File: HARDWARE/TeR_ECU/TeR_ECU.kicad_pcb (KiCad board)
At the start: 4 copper layers, 108.5 x 67.8 mm, 166 parts, among them IC1 MX34040NF2, J1 RJ45_Shielded, J2 RJ45_Shielded, J3 DEBUG, J4 USB_B_Mini, J5 GPS_ANT, K2 G5Q-1, Q1 ZXMN3F30FH, Q2 ZXMN3F30FH, Q3 ZXMN3F30FH, Q4 ZXMN3F30FH, Q5 ZXMN3F30FH, SW1 RST, SW2 BOOT0, U1 TCAN332, U10 NEO-M9N, U11 AT24CS02-STUM, U2 TCAN332, U3 TSR_1-2450, U4 LM1117MP-3.3, U5 LM324, U6 STM32F405VGTx, U7 USBLC6-2SC6, U8 ASM330LHH, U9 LIS3MDL, Y2 ECS-250-20-33-CKM-TR

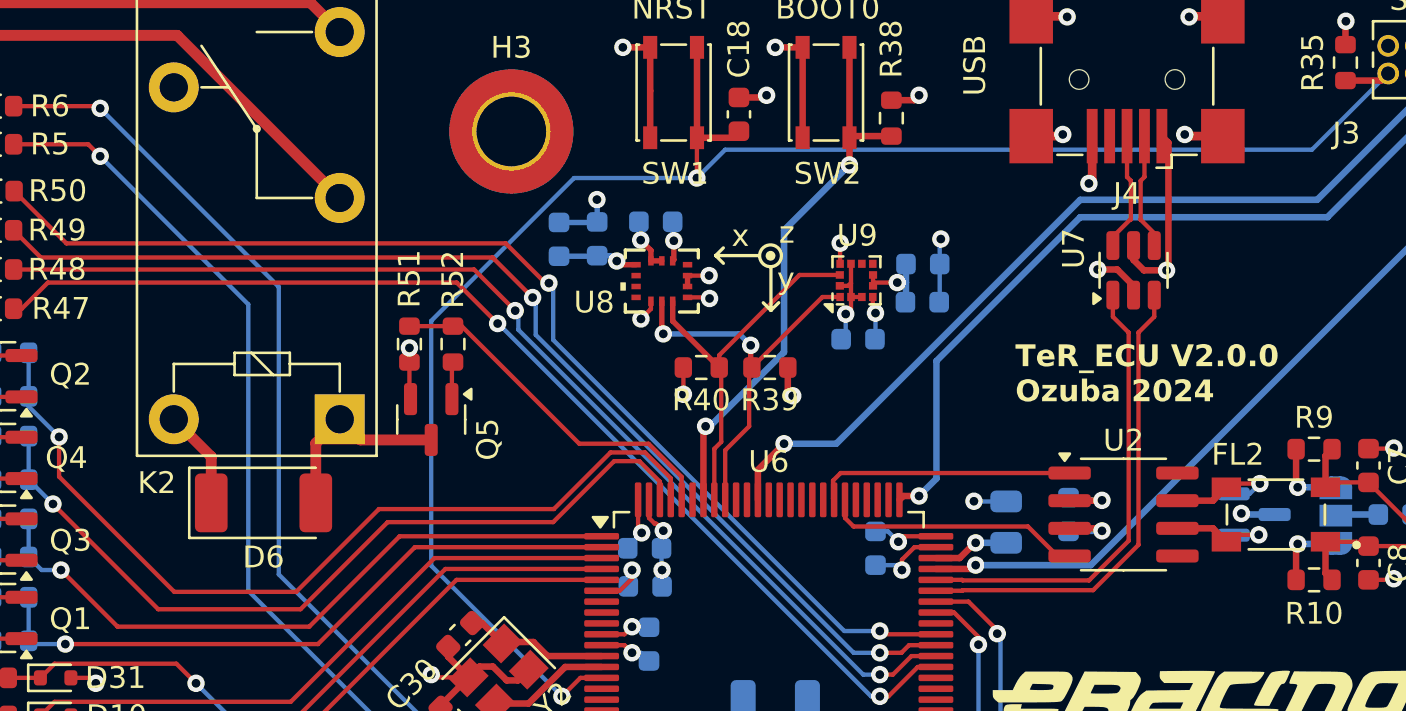
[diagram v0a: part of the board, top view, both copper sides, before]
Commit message: Added Diode to clamp usb pwr
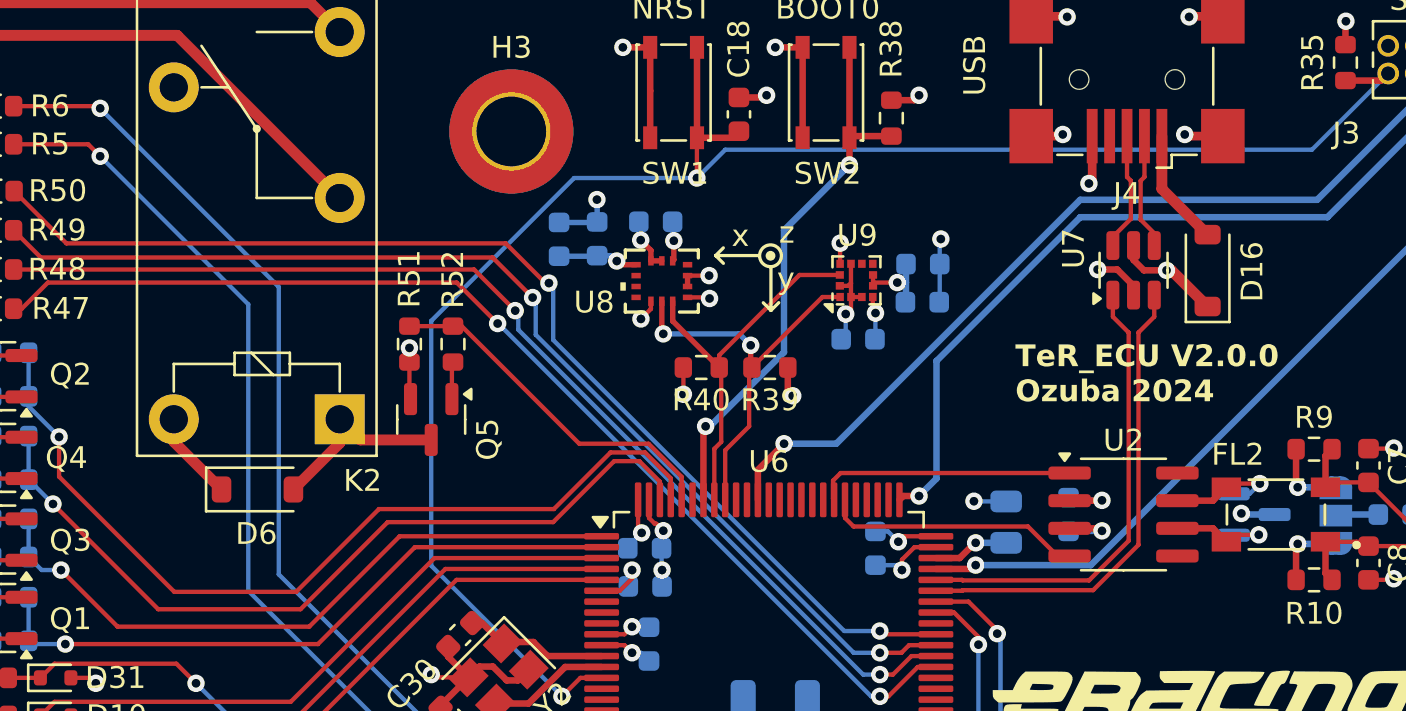
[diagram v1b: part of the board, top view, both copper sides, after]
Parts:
- added D16: SS14, Diode_SMD:D_SOD-123, F.Cu at (170.7, 72.0)
- D6: value SM4007 -> SS14; footprint Diode_SMD:D_MELF -> Diode_SMD:D_SOD-123
- moved D6 0.67 mm to (127.0, 82.1)
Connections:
- J4 pad 1: +5V -> Net-(D16-A)
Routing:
- net Net-(D16-A): track 0.00 -> 5.39 mm
- net +5V: track 143.8 -> 140.1 mm

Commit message: Archivos de producción V2.0.0
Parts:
- D1, D2, D3, D4: footprint LED_SMD:LED_0805_2012Metric -> LED_SMD:LED_0603_1608Metric
- R1, R2, R3, R4: footprint Resistor_SMD:R_0805_2012Metric -> Resistor_SMD:R_0603_1608Metric

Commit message: Added eeprom lib inc path and fixed 120R resistors in Hardware
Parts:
- R10, R7, R8, R9: value 120R -> 60R
